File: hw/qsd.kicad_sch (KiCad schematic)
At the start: 36 parts, among them U1201 SZNUP1105LT1G, U1202 TS3A4751RUCR, U1203 MAX9939AUB+T, U1204 MAX9939AUB+T

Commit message: I think I have finished the relay conversion and 5V SPI I/O expander crap
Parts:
- renumbered C1201 to C7777, C1202 to C7778, C1203 to C7779, C1204 to C7780, C1205 to C7781, C1206 to C7782, C1207 to C7783, C1208 to C7784, C1209 to C7785, C1210 to C7786, C1211 to C7787, C1212 to C7788, C1213 to C7789, C1214 to C7790, C1215 to C7791, C1216 to C7792, C1217 to C7793, C1218 to C7794, C1219 to C7795, R1201 to R7724, R1202 to R7725, R1203 to R7726, R1204 to R7727, R1205 to R7728, R1206 to R7729, R1207 to R7730, R1208 to R7731, R1209 to R7732, R1210 to R7733, R1211 to R7734, R1212 to R7735, R1213 to R7736, U1201 to U7712, U1202 to U7713, U1203 to U7714, U1204 to U7715

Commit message: Starting to build guanella transformers. Mostly converted to 1-2-1 tx, but FPGA still to do.
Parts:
- renumbered C7777 to C7800, C7778 to C7801, C7779 to C7802, C7780 to C7803, C7781 to C7804, C7782 to C7805, C7783 to C7806, C7784 to C7807, C7785 to C7808, C7786 to C7809, C7787 to C7810, C7788 to C7811, C7789 to C7812, C7790 to C7813, C7791 to C7814, C7792 to C7815, C7793 to C7816, C7794 to C7817, C7795 to C7818, U7712 to U7718, U7713 to U7719, U7714 to U7720, U7715 to U7721

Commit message: Checkpoint. FPGA is mostly done (need a check!). Working on new LPFs. Need inductor footprints and to fix a bunch of broken/missing footprints.
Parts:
- C7800: footprint Capacitor_SMD:C_1206_3216Metric -> Capacitor_SMD:C_0603_1608Metric
- C7802, C7812, C7813: footprint Capacitor_SMD:C_0805_2012Metric -> Capacitor_SMD:C_0603_1608Metric
- C7815, C7816, C7817, C7818: footprint Capacitor_SMD:C_0201_0603Metric -> Capacitor_SMD:C_0603_1608Metric
- R7724, R7725, R7726, R7727, R7728, R7729, R7730, R7731, R7732: footprint Resistor_SMD:R_0603_1608Metric -> Resistor_SMD:R_0402_1005Metric
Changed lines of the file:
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@@
 			)
 		)
-		(property "Footprint" "Resistor_SMD:R_0603_1608Metric"
+		(property "Footprint" "Resistor_SMD:R_0402_1005Metric"
 			(at 100.584 87.884 90)
 			(effects
@@
 			)
 		)
-		(property "Footprint" "Capacitor_SMD:C_0805_2012Metric"
+		(property "Footprint" "Capacitor_SMD:C_0603_1608Metric"
 			(at 32.7152 173.99 0)
 			(effects
@@
 			)
 		)
-		(property "Footprint" "Capacitor_SMD:C_0805_2012Metric"
+		(property "Footprint" "Capacitor_SMD:C_0603_1608Metric"
 			(at 129.2352 127 0)
 			(effects
@@
 			)
 		)
-		(property "Footprint" "Capacitor_SMD:C_0201_0603Metric"
+		(property "Footprint" "Capacitor_SMD:C_0603_1608Metric"
 			(at 204.1652 134.62 0)
 			(effects
@@
 			)
 		)
-		(property "Footprint" "Capacitor_SMD:C_0201_0603Metric"
+		(property "Footprint" "Capacitor_SMD:C_0603_1608Metric"
 			(at 204.1652 40.64 0)
 			(effects
@@
 			)
 		)
-		(property "Footprint" "Resistor_SMD:R_0603_1608Metric"
+		(property "Footprint" "Resistor_SMD:R_0402_1005Metric"
 			(at 188.214 39.624 90)
 			(effects
@@
 			)
 		)
-		(property "Footprint" "Resistor_SMD:R_0603_1608Metric"
+		(property "Footprint" "Resistor_SMD:R_0402_1005Metric"
 			(at 105.664 87.884 90)
 			(effects
@@
 			)
 		)
-		(property "Footprint" "Resistor_SMD:R_0603_1608Metric"
+		(property "Footprint" "Resistor_SMD:R_0402_1005Metric"
 			(at 43.434 132.334 90)
 			(effects
@@
 			)
 		)
-		(property "Footprint" "Resistor_SMD:R_0603_1608Metric"
+		(property "Footprint" "Resistor_SMD:R_0402_1005Metric"
 			(at 188.214 117.094 90)
 			(effects
@@
 			)
 		)
-		(property "Footprint" "Capacitor_SMD:C_0805_2012Metric"
+		(property "Footprint" "Capacitor_SMD:C_0603_1608Metric"
 			(at 129.2352 66.04 0)
 			(effects
@@
 			)
 		)
-		(property "Footprint" "Resistor_SMD:R_0603_1608Metric"
+		(property "Footprint" "Resistor_SMD:R_0402_1005Metric"
 			(at 188.214 56.134 90)
 			(effects
@@
 			)
 		)
-		(property "Footprint" "Resistor_SMD:R_0603_1608Metric"
+		(property "Footprint" "Resistor_SMD:R_0402_1005Metric"
 			(at 94.234 28.194 90)
 			(effects
@@
 			)
 		)
-		(property "Footprint" "Capacitor_SMD:C_0201_0603Metric"
+		(property "Footprint" "Capacitor_SMD:C_0603_1608Metric"
 			(at 204.1652 73.66 0)
 			(effects
@@
 			)
 		)
-		(property "Footprint" "Resistor_SMD:R_0603_1608Metric"
+		(property "Footprint" "Resistor_SMD:R_0402_1005Metric"
 			(at 188.214 100.584 90)
 			(effects
@@
 			)
 		)
-		(property "Footprint" "Capacitor_SMD:C_0201_0603Metric"
+		(property "Footprint" "Capacitor_SMD:C_0603_1608Metric"
 			(at 204.1652 101.6 0)
 			(effects
@@
 			)
 		)
-		(property "Footprint" "Capacitor_SMD:C_1206_3216Metric"
+		(property "Footprint" "Capacitor_SMD:C_0603_1608Metric"
 			(at 27.94 143.8148 0)
 			(effects
@@
 			)
 		)
-		(property "Footprint" "Resistor_SMD:R_0603_1608Metric"
+		(property "Footprint" "Resistor_SMD:R_0402_1005Metric"
 			(at 89.154 28.194 90)
 			(effects

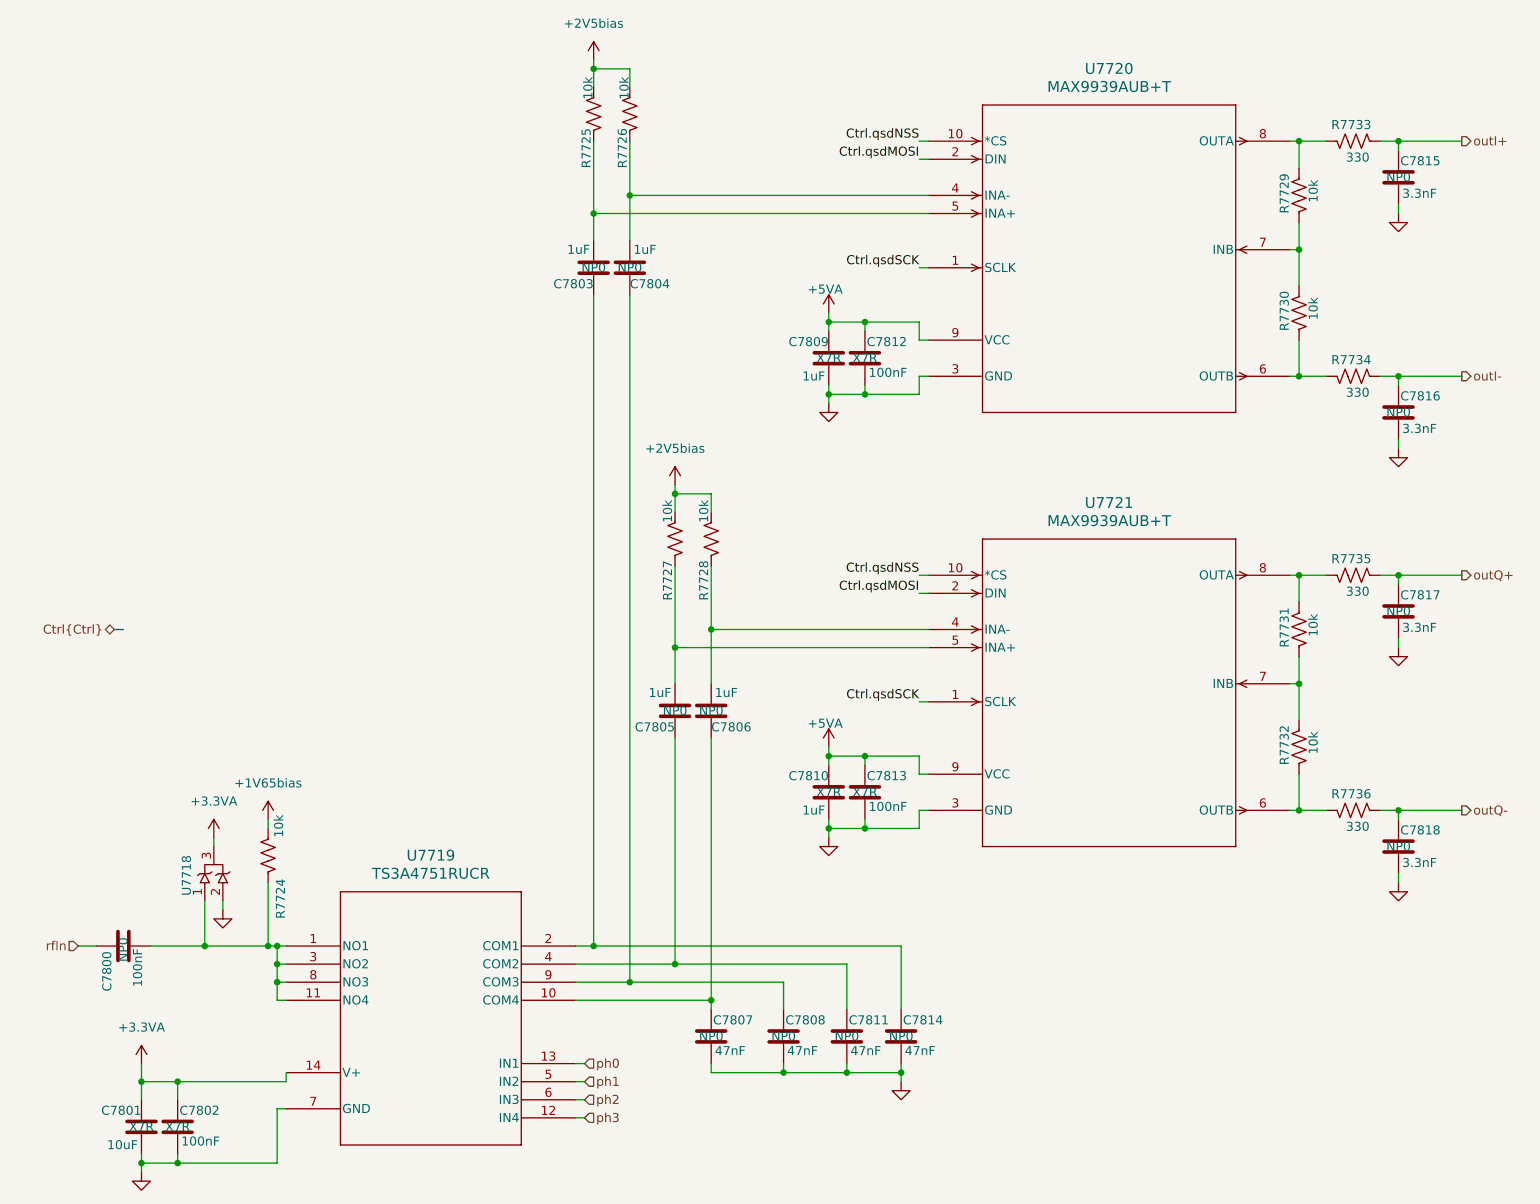
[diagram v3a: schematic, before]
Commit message: OK I have part numbers for consolidated caps, resistors, inductors and all ICs are now Uxxx refdes.
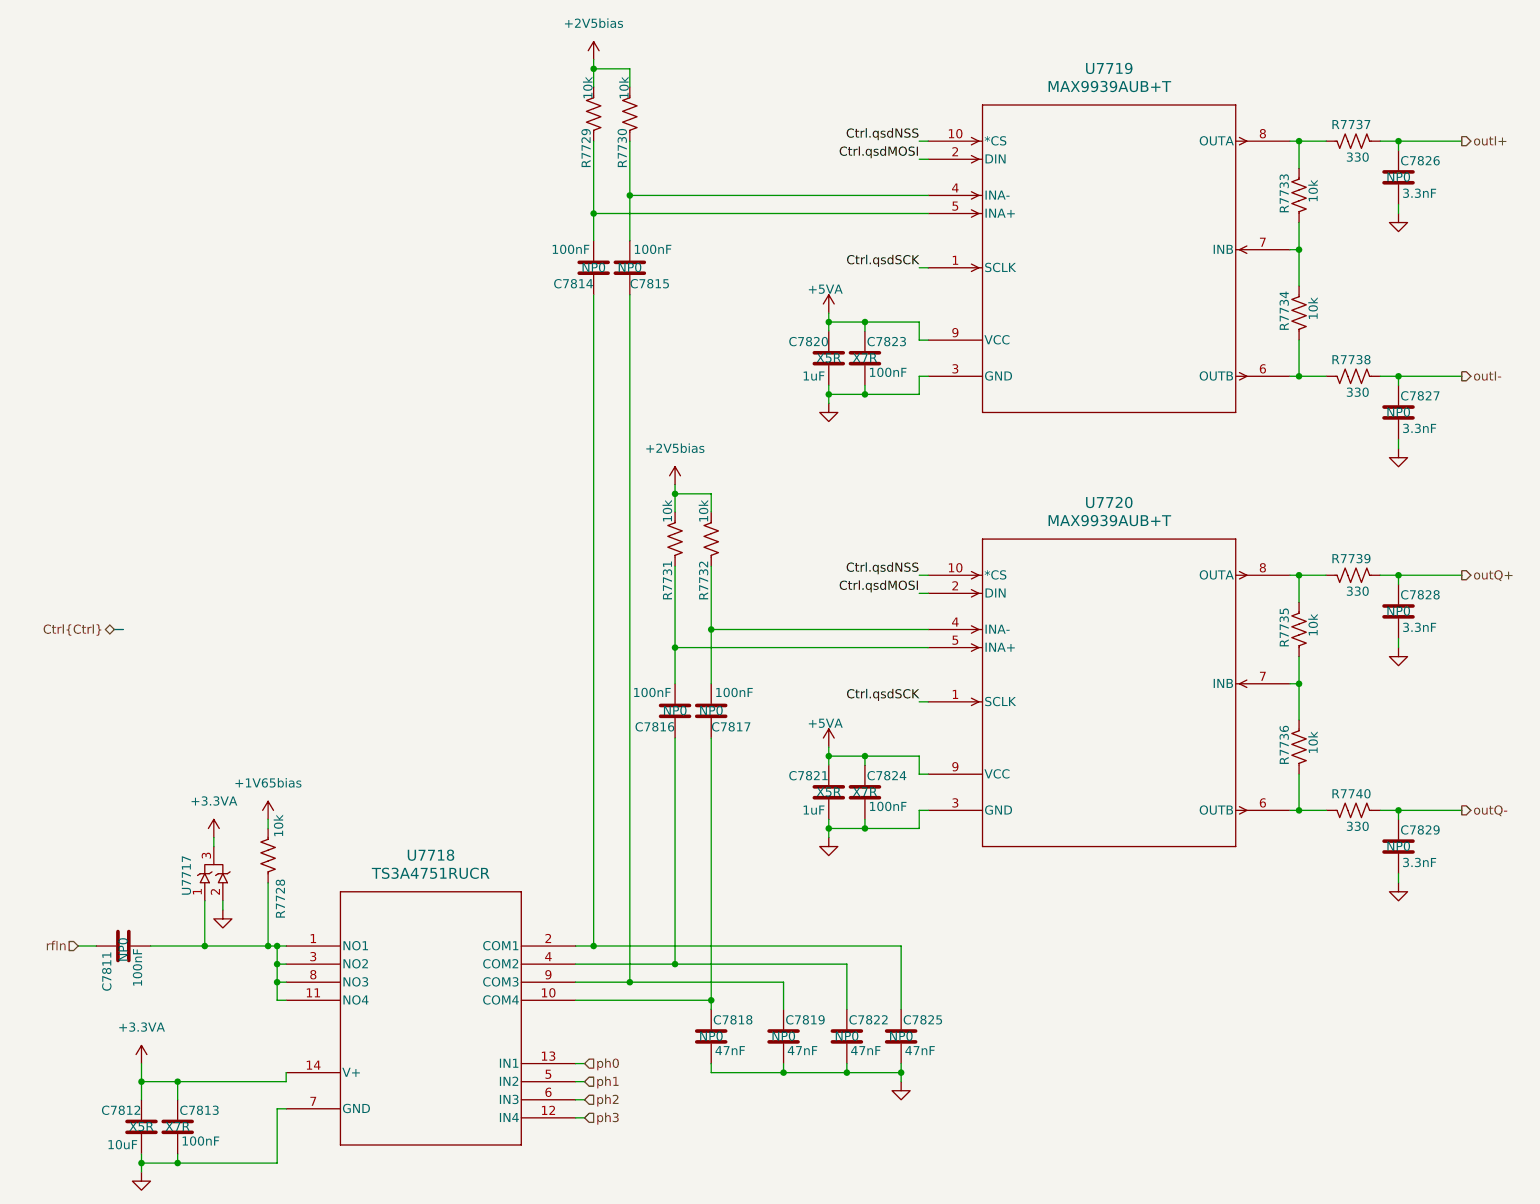
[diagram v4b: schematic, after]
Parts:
- C7811: renamed from C7800; footprint Capacitor_SMD:C_0603_1608Metric -> Capacitor_SMD:C_1206_3216Metric; Manufacturer_Name (none) -> Murata; Manufacturer_Part_Number (none) -> GRM31C5C2A104JA01L; Mouser Part Number (none) -> 81-GRM31C5C2A104JA1L; cap-type NP0 -> NP0; working-voltage 25V -> 50V
- C7812: renamed from C7801; footprint Capacitor_SMD:C_1206_3216Metric -> Capacitor_SMD:C_0603_1608Metric; Manufacturer_Name (none) -> Taoup Uidem; Manufacturer_Part_Number (none) -> 81-GXT155R71E223KE1D; Mouser Part Number (none) -> 963-MLAST168BB5106MT; cap-type X7R -> X5R; working-voltage 10V -> 25V
- C7813: renamed from C7802; Manufacturer_Name (none) -> Kemet; Manufacturer_Part_Number (none) -> C0805F104K1RACAUTO; Mouser Part Number (none) -> 80-C0805F104K1RAUTO
- C7814: renamed from C7803; value 1uF -> 100nF; Manufacturer_Name (none) -> Murata; Manufacturer_Part_Number (none) -> GRM31C5C2A104JA01L; Mouser Part Number (none) -> 81-GRM31C5C2A104JA1L; cap-type NP0 -> NP0; working-voltage 25V -> 50V
- C7815: renamed from C7804; value 1uF -> 100nF; Manufacturer_Name (none) -> Murata; Manufacturer_Part_Number (none) -> GRM31C5C2A104JA01L; Mouser Part Number (none) -> 81-GRM31C5C2A104JA1L; cap-type NP0 -> NP0; working-voltage 25V -> 50V
- C7816: renamed from C7805; value 1uF -> 100nF; Manufacturer_Name (none) -> Murata; Manufacturer_Part_Number (none) -> GRM31C5C2A104JA01L; Mouser Part Number (none) -> 81-GRM31C5C2A104JA1L; cap-type NP0 -> NP0; working-voltage 25V -> 50V
- C7817: renamed from C7806; value 1uF -> 100nF; Manufacturer_Name (none) -> Murata; Manufacturer_Part_Number (none) -> GRM31C5C2A104JA01L; Mouser Part Number (none) -> 81-GRM31C5C2A104JA1L; cap-type NP0 -> NP0; working-voltage 25V -> 50V
- C7818: renamed from C7807; footprint Capacitor_Tantalum_SMD:CP_EIA-3528-21_Kemet-B -> Capacitor_SMD:C_0805_2012Metric; Manufacturer_Name (none) -> Murata; Manufacturer_Part_Number (none) -> GCM31M5C1H473FA16L; Mouser Part Number (none) -> 81-GCM31M5C1H473FA6L
- C7819: renamed from C7808; footprint Capacitor_Tantalum_SMD:CP_EIA-3528-21_Kemet-B -> Capacitor_SMD:C_0805_2012Metric; Manufacturer_Name (none) -> Murata; Manufacturer_Part_Number (none) -> GCM31M5C1H473FA16L; Mouser Part Number (none) -> 81-GCM31M5C1H473FA6L
- C7820: renamed from C7809; footprint Capacitor_SMD:C_1206_3216Metric -> Capacitor_SMD:C_0402_1005Metric; Manufacturer_Name (none) -> Murata; Manufacturer_Part_Number (none) -> GRM155R61E105KE11D; Mouser Part Number (none) -> 81-GRM155R61E105KE1D; cap-type X7R -> X5R
- C7821: renamed from C7810; footprint Capacitor_SMD:C_1206_3216Metric -> Capacitor_SMD:C_0402_1005Metric; Manufacturer_Name (none) -> Murata; Manufacturer_Part_Number (none) -> GRM155R61E105KE11D; Mouser Part Number (none) -> 81-GRM155R61E105KE1D; cap-type X7R -> X5R
- C7822: renamed from C7811; footprint Capacitor_Tantalum_SMD:CP_EIA-3528-21_Kemet-B -> Capacitor_SMD:C_0805_2012Metric; Manufacturer_Name (none) -> Murata; Manufacturer_Part_Number (none) -> GCM31M5C1H473FA16L; Mouser Part Number (none) -> 81-GCM31M5C1H473FA6L
- C7823: renamed from C7812; Manufacturer_Name (none) -> Kemet; Manufacturer_Part_Number (none) -> C0805F104K1RACAUTO; Mouser Part Number (none) -> 80-C0805F104K1RAUTO
- C7824: renamed from C7813; Manufacturer_Name (none) -> Kemet; Manufacturer_Part_Number (none) -> C0805F104K1RACAUTO; Mouser Part Number (none) -> 80-C0805F104K1RAUTO
- C7825: renamed from C7814; footprint Capacitor_Tantalum_SMD:CP_EIA-3528-21_Kemet-B -> Capacitor_SMD:C_0805_2012Metric; Manufacturer_Name (none) -> Murata; Manufacturer_Part_Number (none) -> GCM31M5C1H473FA16L; Mouser Part Number (none) -> 81-GCM31M5C1H473FA6L
- C7826: renamed from C7815; Manufacturer_Name (none) -> TDK; Manufacturer_Part_Number (none) -> C1608C0G1H332J080AE; Mouser Part Number (none) -> 810-C1608C0G1H332J08
- C7827: renamed from C7816; Manufacturer_Name (none) -> TDK; Manufacturer_Part_Number (none) -> C1608C0G1H332J080AE; Mouser Part Number (none) -> 810-C1608C0G1H332J08
- C7828: renamed from C7817; Manufacturer_Name (none) -> TDK; Manufacturer_Part_Number (none) -> C1608C0G1H332J080AE; Mouser Part Number (none) -> 810-C1608C0G1H332J08
- C7829: renamed from C7818; Manufacturer_Name (none) -> TDK; Manufacturer_Part_Number (none) -> C1608C0G1H332J080AE; Mouser Part Number (none) -> 810-C1608C0G1H332J08
- renumbered R7724 to R7728, R7725 to R7729, R7726 to R7730, R7727 to R7731, R7728 to R7732, R7729 to R7733, R7730 to R7734, R7731 to R7735, R7732 to R7736, R7733 to R7737, R7734 to R7738, R7735 to R7739, R7736 to R7740, U7718 to U7717, U7719 to U7718, U7720 to U7719, U7721 to U7720

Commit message: All symbols and footprints seem right now, and schematic again imports into PCB without error
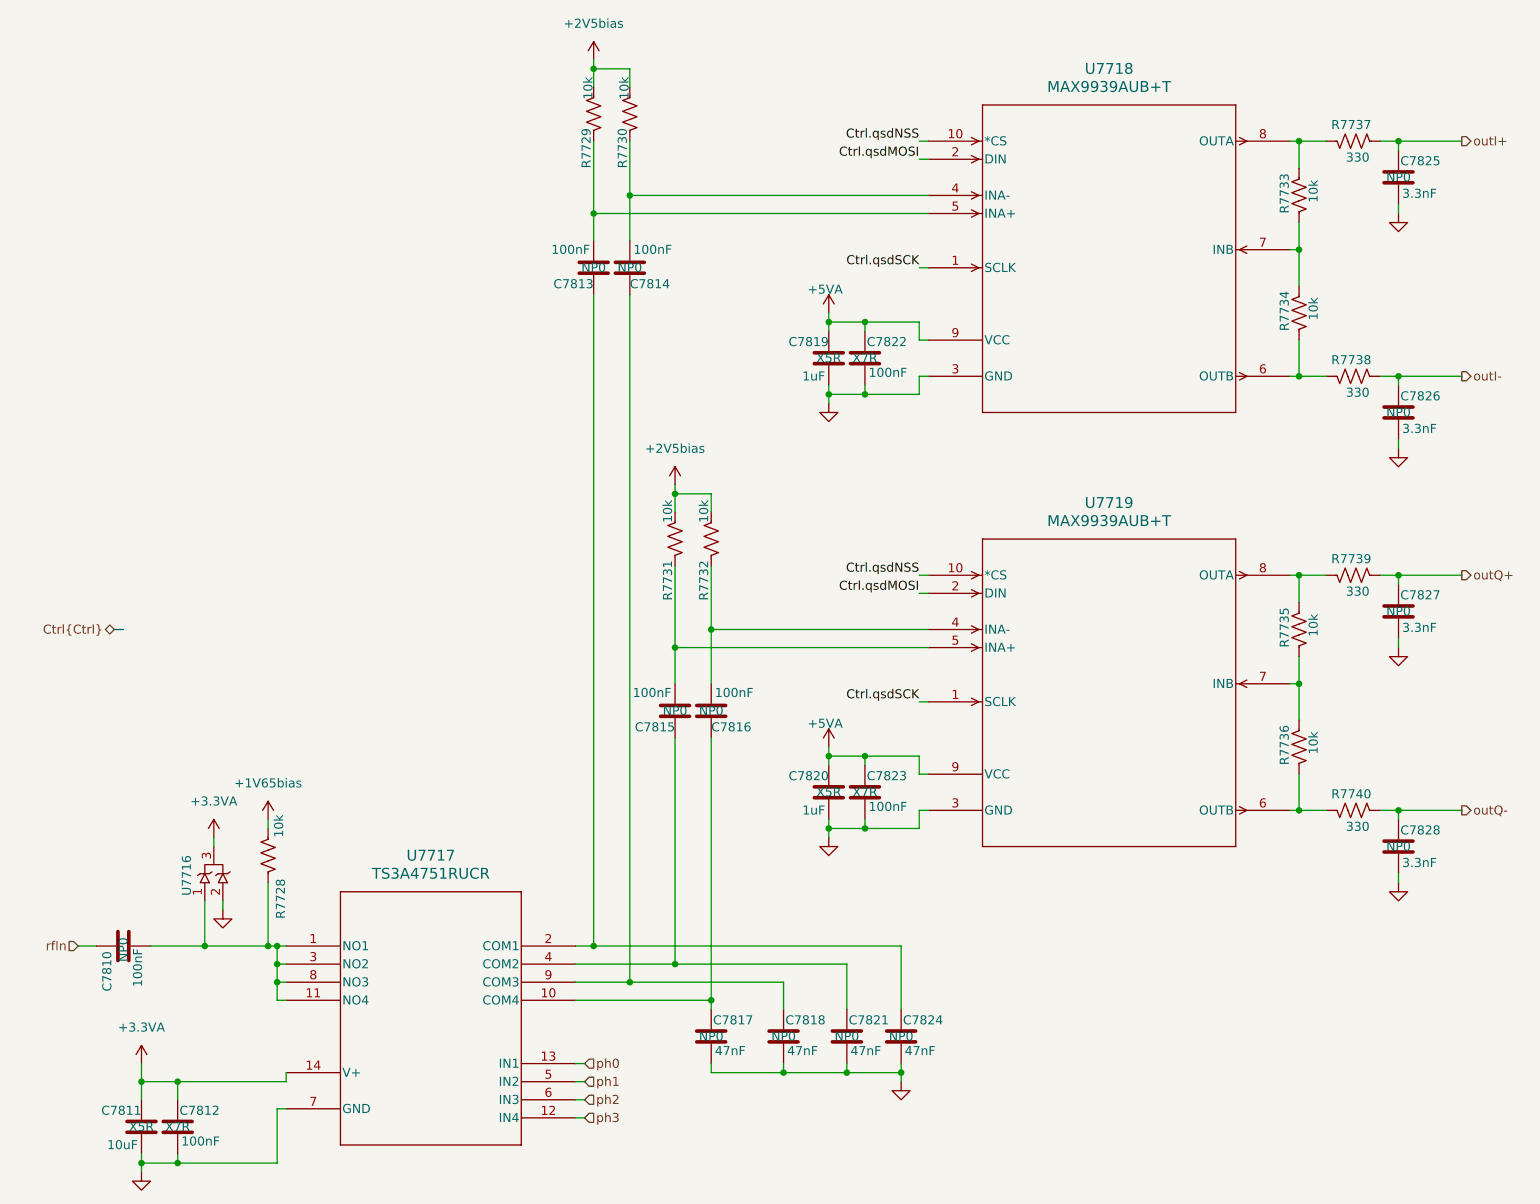
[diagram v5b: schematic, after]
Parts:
- U7717: renamed from U7718; footprint RUC14 -> Library:TS3A4751-RUC14
- renumbered C7811 to C7810, C7812 to C7811, C7813 to C7812, C7814 to C7813, C7815 to C7814, C7816 to C7815, C7817 to C7816, C7818 to C7817, C7819 to C7818, C7820 to C7819, C7821 to C7820, C7822 to C7821, C7823 to C7822, C7824 to C7823, C7825 to C7824, C7826 to C7825, C7827 to C7826, C7828 to C7827, C7829 to C7828, U7717 to U7716, U7719 to U7718, U7720 to U7719

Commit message: I'm thinking I might make a NexRx with just the rx portion of this design first to test my skills and capabilities.
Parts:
- renumbered C7810 to C7809, C7811 to C7810, C7812 to C7811, C7813 to C7812, C7814 to C7813, C7815 to C7814, C7816 to C7815, C7817 to C7816, C7818 to C7817, C7819 to C7818, C7820 to C7819, C7821 to C7820, C7822 to C7821, C7823 to C7822, C7824 to C7823, C7825 to C7824, C7826 to C7825, C7827 to C7826, C7828 to C7827

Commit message: Off to a great start building just the NexRx
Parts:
- renumbered C7809 to C1201, C7810 to C1202, C7811 to C1203, C7812 to C1204, C7813 to C1205, C7814 to C1206, C7815 to C1207, C7816 to C1208, C7817 to C1209, C7818 to C1210, C7819 to C1211, C7820 to C1212, C7821 to C1213, C7822 to C1214, C7823 to C1215, C7824 to C1216, C7825 to C1217, C7826 to C1218, C7827 to C1219, R7728 to R1201, R7729 to R1202, R7730 to R1203, R7731 to R1204, R7732 to R1205, R7733 to R1206, R7734 to R1207, R7735 to R1208, R7736 to R1209, R7737 to R1210, R7738 to R1211, R7739 to R1212, R7740 to R1213, U7716 to U1201, U7717 to U1202, U7718 to U1203, U7719 to U1204

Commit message: All ERC pass. Import to PCB works with no footprints missing.
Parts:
- U1203, U1204: symbol MAX9939AUB:MAX9939AUB+T -> Library:MAX9939AUB+T
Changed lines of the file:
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@@
 			)
 		)
+		(property "cap-type" ""
+			(at 36.83 135.89 0)
+			(effects
+				(font
+					(size 1.27 1.27)
+				)
+			)
+		)
+		(property "r-power" ""
+			(at 36.83 135.89 0)
+			(effects
+				(font
+					(size 1.27 1.27)
+				)
+			)
+		)
 		(pin "3"
 		)
@@
 	)
 	(symbol
-		(lib_name "MAX9939AUB+T_2")
-		(lib_id "MAX9939AUB:MAX9939AUB+T")
+		(lib_id "Library:MAX9939AUB+T")
 		(at 137.16 31.75 0)
 		(unit 1)
@@
 	)
 	(symbol
-		(lib_name "MAX9939AUB+T_2")
-		(lib_id "MAX9939AUB:MAX9939AUB+T")
+		(lib_id "Library:MAX9939AUB+T")
 		(at 137.16 92.71 0)
 		(unit 1)
